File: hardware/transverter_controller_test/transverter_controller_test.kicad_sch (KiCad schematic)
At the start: 43 parts, among them J1 CNC Tech 3020-10-0200-00‎, J2 USB_C_Receptacle_USB2.0, J3 Conn_01x03_Male, J4 CNC Tech 3020-10-0200-00‎, M1 Logo_10mmx10mm, Q1 DMN62D0U-13, Q2 DMN62D0U-13, U1 PCT2075D, U2 24LC024-I/SN, U3 MKL26Z64VFT4, U4 MAX3483ESA+, Y1 830108178109

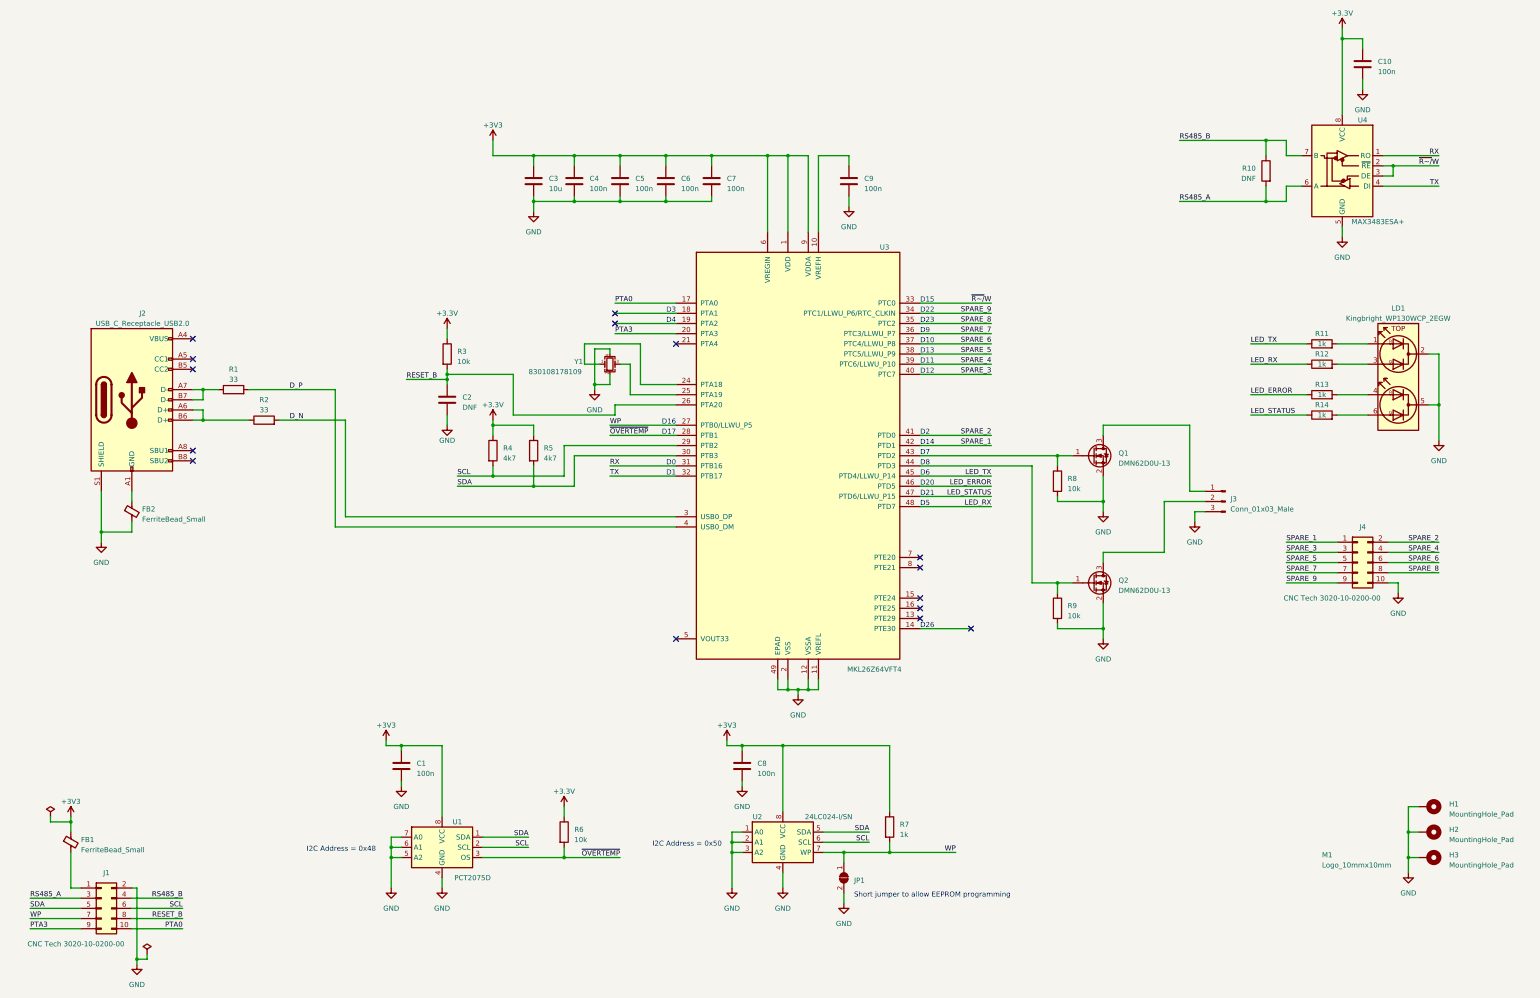
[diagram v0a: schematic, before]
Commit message: Added RS485 test board
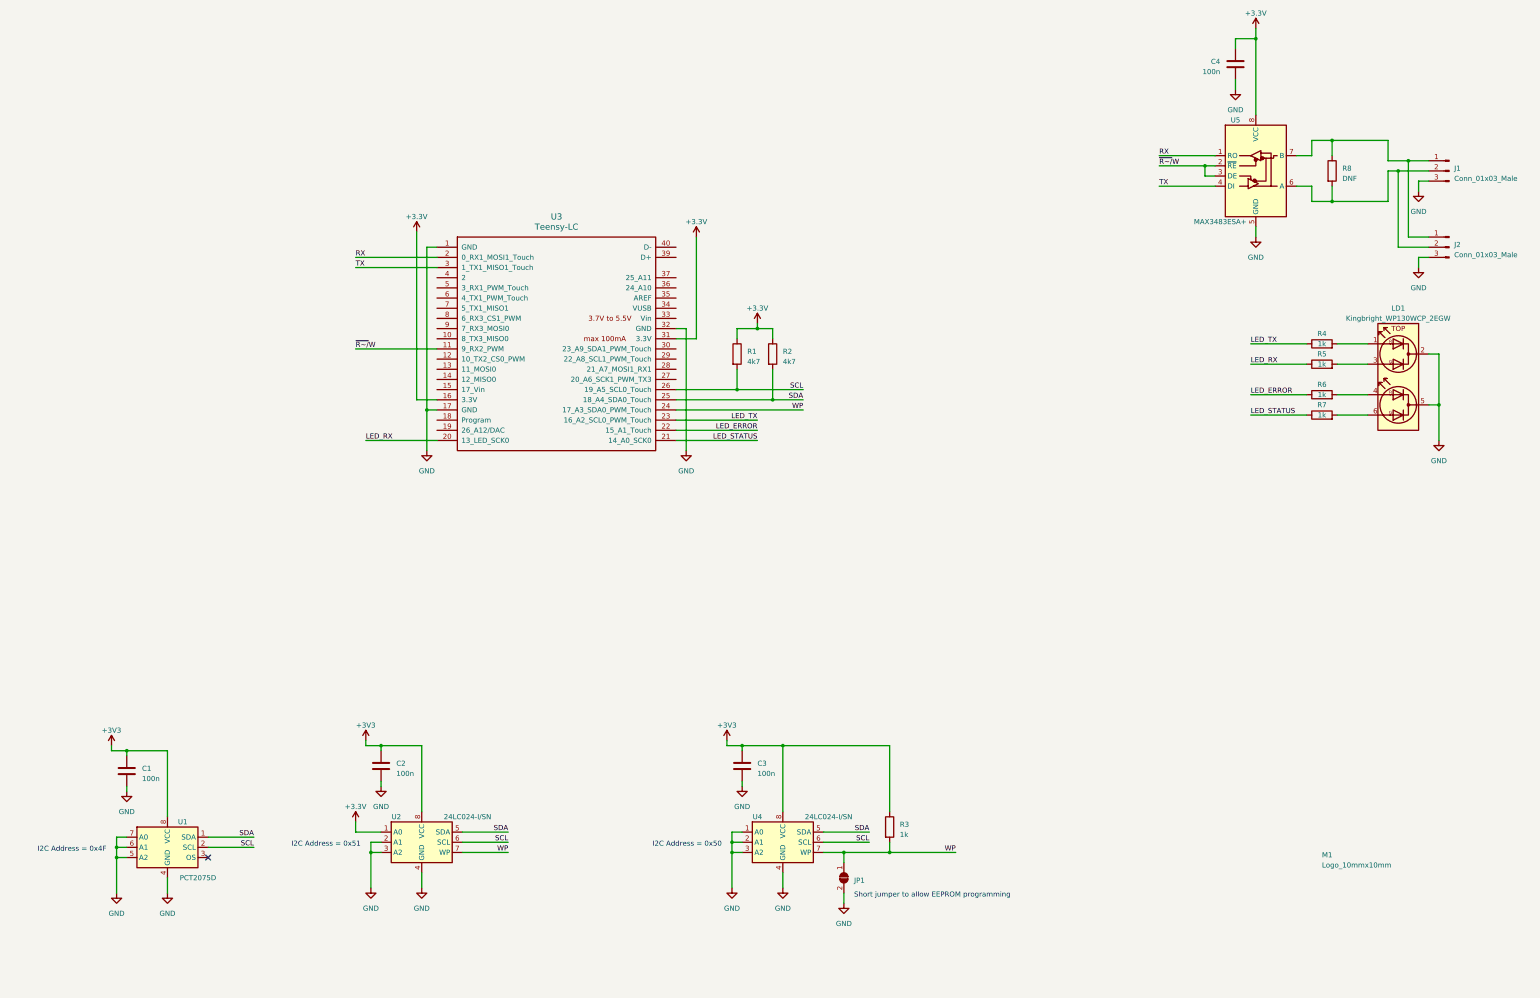
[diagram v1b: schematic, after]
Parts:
- removed C3: 10u, Capacitor_SMD:C_0603_1608Metric, symbol Device:C
- removed C4, C5, C6, C7, C9: 100n, Capacitor_SMD:C_0402_1005Metric, symbol Device:C
- removed FB1, FB2: FerriteBead_Small, Inductor_SMD:L_0603_1608Metric, symbol Device:FerriteBead_Small
- removed H1, H2, H3: MountingHole_Pad, MountingHole:MountingHole_3.2mm_M3_Pad_Via, symbol Mechanical:MountingHole_Pad
- removed J1, J4: CNC Tech 3020-10-0200-00‎, Connector_WUT:Header_CNC-Tech_3020-10-0200-00_2x5_TH_RA, symbol Connector_Generic:Conn_02x05_Odd_Even
- removed J2: USB_C_Receptacle_USB2.0, Connector_WUT:USB-C_HRO_TYPE-C-31-M-12, symbol Connector:USB_C_Receptacle_USB2.0
- removed J3: Conn_01x03_Male, Connector_PinHeader_2.54mm:PinHeader_1x03_P2.54mm_Vertical, symbol Connector:Conn_01x03_Male
- removed Q1, Q2: DMN62D0U-13, Package_TO_SOT_SMD:SOT-23, symbol Device:Q_NMOS_GSD
- removed R3, R6, R8, R9: 10k, Resistor_SMD:R_0402_1005Metric, symbol Device:R
- removed R4, R5: 4k7, Resistor_SMD:R_0402_1005Metric, symbol Device:R
- removed U3: MKL26Z64VFT4, Package_DFN_QFN:QFN-48-1EP_7x7mm_P0.5mm_EP5.15x5.15mm, symbol MCU_NXP_Kinetis:MKL26Z64VFT4
- removed Y1: 830108178109, Crystal:Crystal_SMD_2016-4Pin_2.0x1.6mm, symbol Device:Crystal_GND24_Small
- added J1, J2: Conn_01x03_Male, Connector_JST:JST_PH_B3B-PH-K_1x03_P2.00mm_Vertical, symbol Connector:Conn_01x03_Male
- added U2: 24LC024-I/SN, Package_SO:SO-8_3.9x4.9mm_P1.27mm, symbol Memory_EEPROM:24LC02
- added U3: Teensy-LC, teensy:Teensy_LC, symbol teensy:Teensy-LC
- C2: value DNF -> 100n
- R1, R2: value 33 -> 4k7
- renumbered C8 to C3, C10 to C4, R7 to R3, R11 to R4, R12 to R5, R13 to R6, R14 to R7, R10 to R8, U2 to U4, U4 to U5
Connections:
- net D_N is gone; now on net SDA: R2.2
- net D_P is gone; now on net SCL: R1.2
- net RESET_B is gone; now on net +3V3: C2.1
- net +3V3: now also R1.1, R2.1, U2.1 (A0), U2.8 (VCC), U3.16 (3.3V), U3.31 (3.3V)
- net GND: now also J1.3 (Pin_3), J2.3 (Pin_3), U2.2 (A1), U2.3 (A2), U2.4 (GND), U3.1 (GND), U3.17 (GND), U3.32 (GND)
- net LED_ERROR: now also U3.22 (15_A1_Touch)
- net LED_RX: now also U3.20 (13_LED_SCK0)
- net LED_STATUS: now also U3.21 (14_A0_SCK0)
- net LED_TX: now also U3.23 (16_A2_SCL0_PWM_Touch)
- net RX: now also U3.2 (0_RX1_MOSI1_Touch)
- net SCL: now also U2.6 (SCL), U3.26 (19_A5_SCL0_Touch)
- net SDA: now also U2.5 (SDA), U3.25 (18_A4_SDA0_Touch)
- net TX: now also U3.3 (1_TX1_MISO1_Touch)
- net WP: now also U2.7 (WP), U3.24 (17_A3_SDA0_PWM_Touch)
- net ~R~/W: now also U3.11 (9_RX2_PWM)
- net RS485_A: no longer names the net of R8.2, U5.6 (A)
- net RS485_A: now also J1.2 (Pin_2), J2.2 (Pin_2)
- net RS485_B: no longer names the net of R8.1, U5.7 (B)
- net RS485_B: now also J1.1 (Pin_1), J2.1 (Pin_1)
- net ~OVERTEMP: no longer names the net of U1.3 (OS)
- no-connect marks 15 -> 1
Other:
- note added: "I2C Address = 0x4F"
- note added: "I2C Address = 0x51"
- note removed: "D0"
- note removed: "D1"
- note removed: "D10"
- note removed: "D11"
- note removed: "D12"
- note removed: "D13"
- note removed: "D14"
- note removed: "D15"
- note removed: "D16"
- note removed: "D17"
- note removed: "D2"
- note removed: "D20"
- note removed: "D21"
- note removed: "D22"
- note removed: "D23"
- note removed: "D26"
- note removed: "D3"
- note removed: "D4"
- note removed: "D5"
- note removed: "D6"
- note removed: "D7"
- note removed: "D8"
- note removed: "D9"
- note removed: "I2C Address = 0x48"
- moved on the sheet: C4, R8, U5

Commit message: Got temperature sensor working
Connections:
- net ~R~/W renamed ~{R}/W
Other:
- note added: "I2C Address = 0x48"
- note removed: "I2C Address = 0x4F"
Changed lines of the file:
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@@
-(kicad_sch (version 20210406) (generator eeschema)
+(kicad_sch (version 20210606) (generator eeschema)
   (paper "A3")
   (junction (at 45.72 234.95) (diameter 0.9144) (color 0 0 0 0))
@@
     (stroke (width 0) (type solid) (color 0 0 0 0))
   )
-  (text "I2C Address = 0x4F" (at 43.18 236.22 180)
+  (text "I2C Address = 0x48" (at 43.18 236.22 180)
     (effects (font (size 1.27 1.27)) (justify right bottom))
   )
@@
     (effects (font (size 1.27 1.27)) (justify left bottom))
   )
-  (label "~R~{slash}W" (at 105.41 110.49 0)
+  (label "~{R}{slash}W" (at 105.41 110.49 0)
     (effects (font (size 1.27 1.27)) (justify left bottom))
   )
@@
     (effects (font (size 1.27 1.27)) (justify left bottom))
   )
-  (label "~R~{slash}W" (at 306.07 64.77 0)
-    (effects (font (size 1.27 1.27)) (justify left bottom))
-  )
+  (label "~{R}{slash}W" (at 306.07 64.77 0)
+    (effects (font (size 1.27 1.27)) (justify left bottom))
+  )
